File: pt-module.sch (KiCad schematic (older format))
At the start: 6 parts

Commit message: Added USB to UART interface
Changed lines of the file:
@@
 LIBS:switches
 LIBS:ESD_Protection
+LIBS:ftdi
 LIBS:pt-module-cache
 EELAYER 25 0
@@
 $Descr A4 11693 8268
 encoding utf-8
-Sheet 1 7
+Sheet 1 8
 Title "ProbeTester Module"
 Date ""
@@
 F4 "termination_logic" I R 9000 4200 60
 $EndSheet
+$Sheet
+S 5400 4550 600  550
+U 59836BB9
+F0 "PT module USB interface" 60
+F1 "pt-module-usb-interface.sch" 60
+$EndSheet
 $EndSCHEMATC

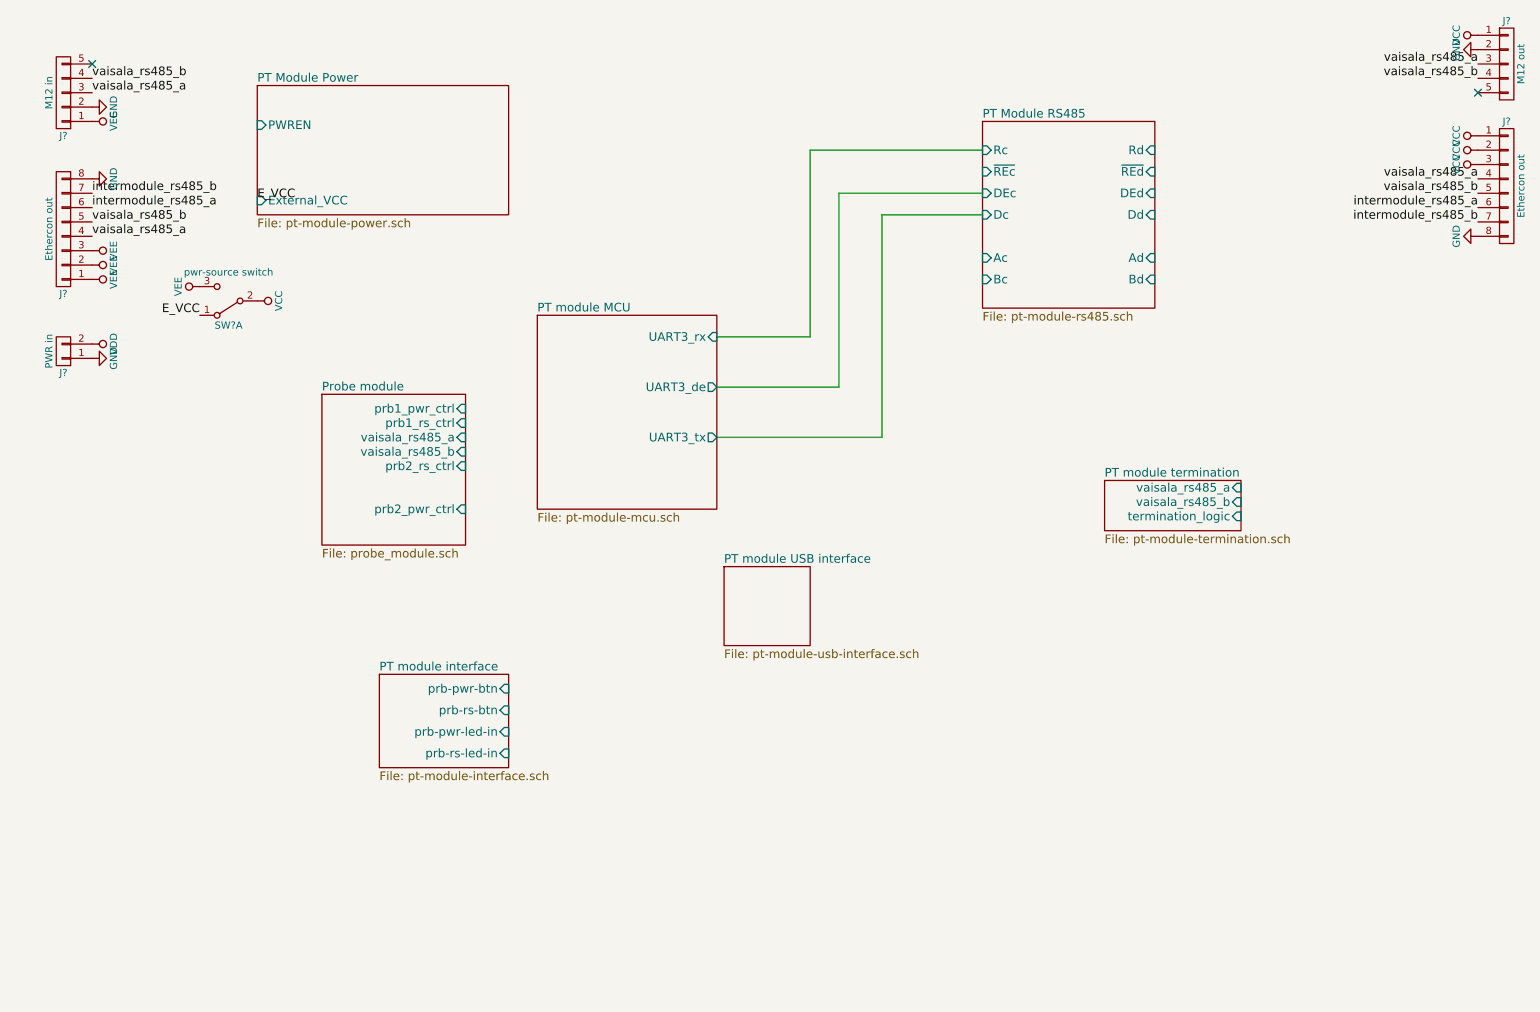
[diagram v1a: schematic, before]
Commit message: Added USB UART hierarchical connection
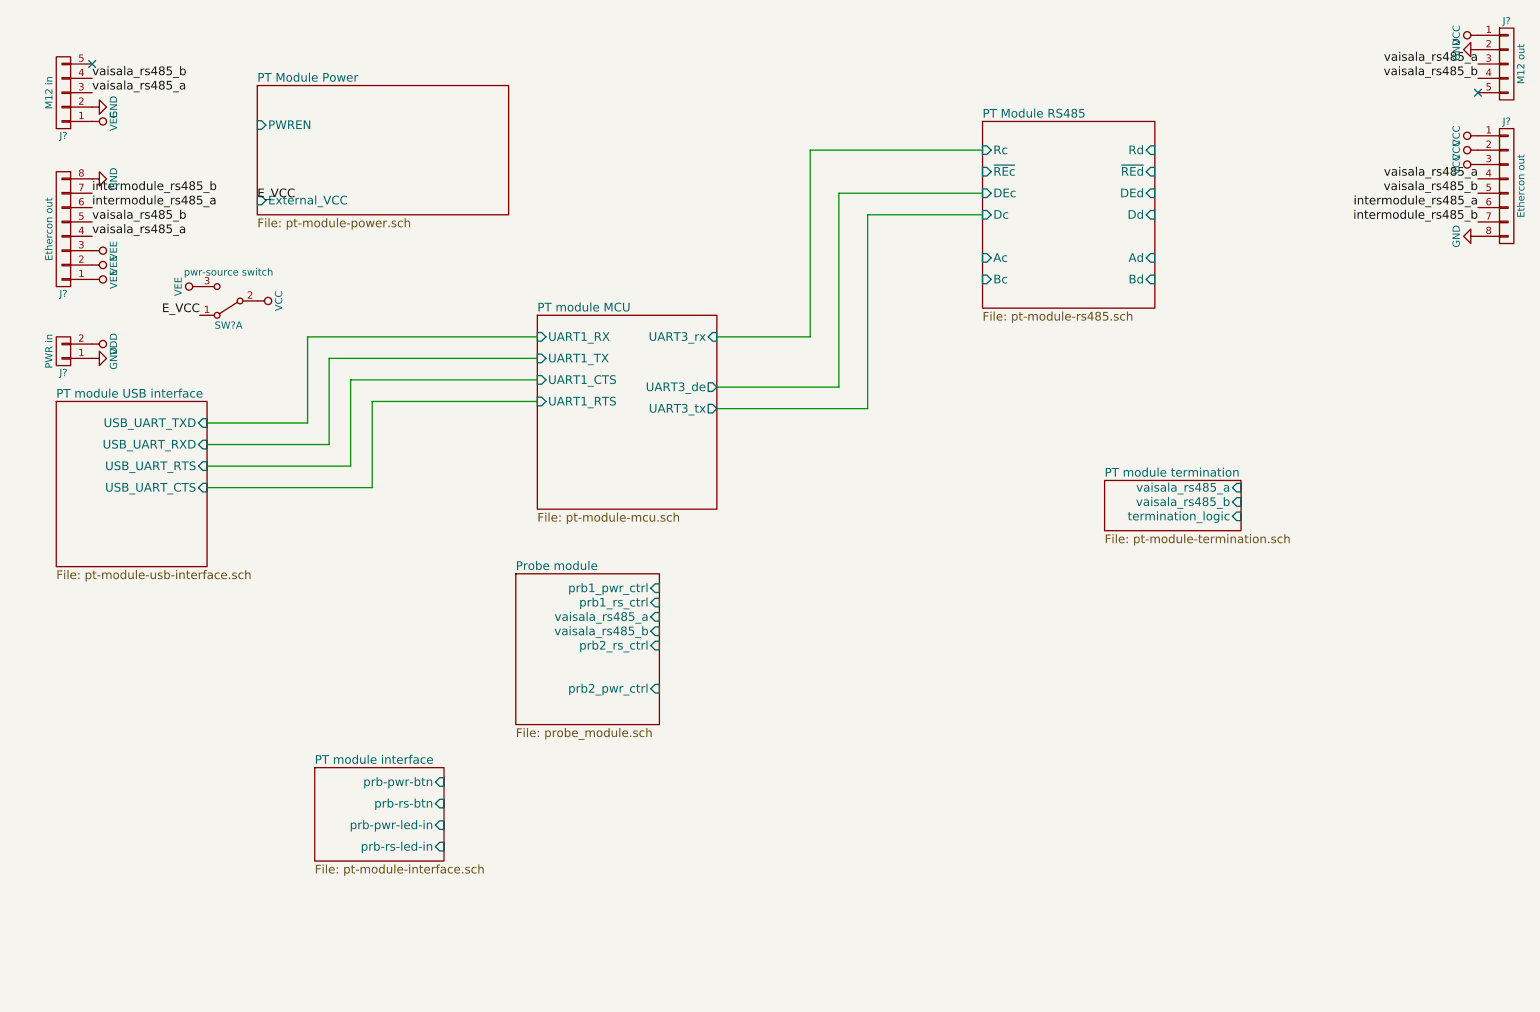
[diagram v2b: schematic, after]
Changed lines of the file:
@@
 F0 "PT module MCU" 60
 F1 "pt-module-mcu.sch" 60
-F2 "UART3_tx" O R 5350 3650 60
+F2 "UART3_tx" O R 5350 3450 60
 F3 "UART3_rx" I R 5350 2950 60
 F4 "UART3_de" O R 5350 3300 60
+F5 "UART1_TX" I L 4100 3100 60
+F6 "UART1_RX" I L 4100 2950 60
+F7 "UART1_CTS" I L 4100 3250 60
+F8 "UART1_RTS" I L 4100 3400 60
 $EndSheet
 $Sheet
-S 2600 3350 1000 1050
+S 3950 4600 1000 1050
 U 598183C5
 F0 "Probe module" 60
 F1 "probe_module.sch" 60
-F2 "prb1_pwr_ctrl" I R 3600 3450 60
-F3 "prb1_rs_ctrl" I R 3600 3550 60
-F4 "prb2_rs_ctrl" I R 3600 3850 60
-F5 "prb2_pwr_ctrl" I R 3600 4150 60
-F6 "vaisala_rs485_a" I R 3600 3650 60
-F7 "vaisala_rs485_b" I R 3600 3750 60
+F2 "prb1_pwr_ctrl" I R 4950 4700 60
+F3 "prb1_rs_ctrl" I R 4950 4800 60
+F4 "prb2_rs_ctrl" I R 4950 5100 60
+F5 "prb2_pwr_ctrl" I R 4950 5400 60
+F6 "vaisala_rs485_a" I R 4950 4900 60
+F7 "vaisala_rs485_b" I R 4950 5000 60
 $EndSheet
 $Sheet
-S 3000 5300 900  650
+S 2550 5950 900  650
 U 59819805
 F0 "PT module interface" 60
 F1 "pt-module-interface.sch" 60
-F2 "prb-pwr-btn" I R 3900 5400 60
-F3 "prb-rs-btn" I R 3900 5550 60
-F4 "prb-pwr-led-in" I R 3900 5700 60
-F5 "prb-rs-led-in" I R 3900 5850 60
+F2 "prb-pwr-btn" I R 3450 6050 60
+F3 "prb-rs-btn" I R 3450 6200 60
+F4 "prb-pwr-led-in" I R 3450 6350 60
+F5 "prb-rs-led-in" I R 3450 6500 60
 $EndSheet
 $Comp
@@
 	6000 1650 7200 1650
 Wire Wire Line
-	5350 3650 6500 3650
-Wire Wire Line
-	6500 3650 6500 2100
-Wire Wire Line
-	6500 2100 7200 2100
+	6400 2100 7200 2100
 Text Label 2150 2000 0    60   ~ 0
 E_VCC
@@
 $EndSheet
 $Sheet
-S 5400 4550 600  550
+S 750  3400 1050 1150
 U 59836BB9
 F0 "PT module USB interface" 60
 F1 "pt-module-usb-interface.sch" 60
-$EndSheet
+F2 "USB_UART_TXD" I R 1800 3550 60
+F3 "USB_UART_RXD" I R 1800 3700 60
+F4 "USB_UART_RTS" I R 1800 3850 60
+F5 "USB_UART_CTS" I R 1800 4000 60
+$EndSheet
+Wire Wire Line
+	6400 2100 6400 3450
+Wire Wire Line
+	6400 3450 5350 3450
+Wire Wire Line
+	2500 2950 4100 2950
+Wire Wire Line
+	2500 2950 2500 3550
+Wire Wire Line
+	2500 3550 1800 3550
+Wire Wire Line
+	4100 3100 2650 3100
+Wire Wire Line
+	2650 3100 2650 3700
+Wire Wire Line
+	2650 3700 1800 3700
+Wire Wire Line
+	4100 3250 2800 3250
+Wire Wire Line
+	2800 3250 2800 3850
+Wire Wire Line
+	2800 3850 1800 3850
+Wire Wire Line
+	4100 3400 2950 3400
+Wire Wire Line
+	2950 3400 2950 4000
+Wire Wire Line
+	2950 4000 1800 4000
 $EndSCHEMATC

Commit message: Added another rs485 link to MCU
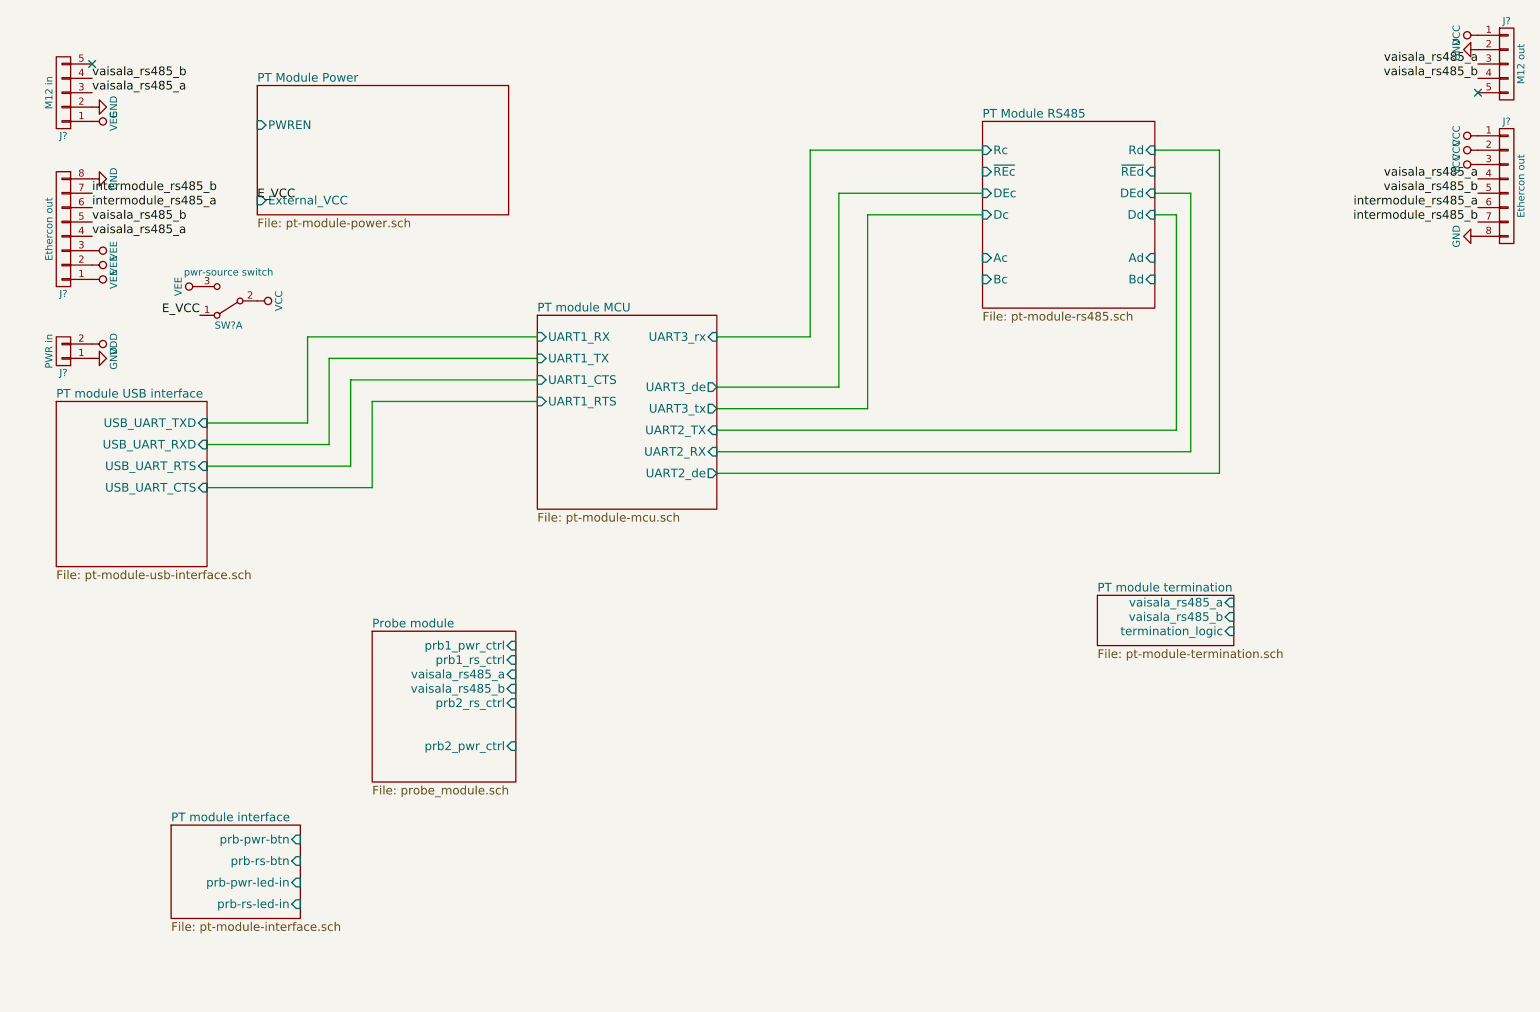
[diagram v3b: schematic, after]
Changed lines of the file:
@@
 F7 "UART1_CTS" I L 4100 3250 60
 F8 "UART1_RTS" I L 4100 3400 60
+F9 "UART2_RX" I R 5350 3750 60
+F10 "UART2_TX" I R 5350 3600 60
+F11 "UART2_de" O R 5350 3900 60
 $EndSheet
 $Sheet
-S 3950 4600 1000 1050
+S 2950 5000 1000 1050
 U 598183C5
 F0 "Probe module" 60
 F1 "probe_module.sch" 60
-F2 "prb1_pwr_ctrl" I R 4950 4700 60
-F3 "prb1_rs_ctrl" I R 4950 4800 60
-F4 "prb2_rs_ctrl" I R 4950 5100 60
-F5 "prb2_pwr_ctrl" I R 4950 5400 60
-F6 "vaisala_rs485_a" I R 4950 4900 60
-F7 "vaisala_rs485_b" I R 4950 5000 60
+F2 "prb1_pwr_ctrl" I R 3950 5100 60
+F3 "prb1_rs_ctrl" I R 3950 5200 60
+F4 "prb2_rs_ctrl" I R 3950 5500 60
+F5 "prb2_pwr_ctrl" I R 3950 5800 60
+F6 "vaisala_rs485_a" I R 3950 5300 60
+F7 "vaisala_rs485_b" I R 3950 5400 60
 $EndSheet
 $Sheet
-S 2550 5950 900  650
+S 1550 6350 900  650
 U 59819805
 F0 "PT module interface" 60
 F1 "pt-module-interface.sch" 60
-F2 "prb-pwr-btn" I R 3450 6050 60
-F3 "prb-rs-btn" I R 3450 6200 60
-F4 "prb-pwr-led-in" I R 3450 6350 60
-F5 "prb-rs-led-in" I R 3450 6500 60
+F2 "prb-pwr-btn" I R 2450 6450 60
+F3 "prb-rs-btn" I R 2450 6600 60
+F4 "prb-pwr-led-in" I R 2450 6750 60
+F5 "prb-rs-led-in" I R 2450 6900 60
 $EndSheet
 $Comp
@@
 $EndComp
 $Sheet
-S 8050 3950 950  350
+S 8000 4750 950  350
 U 5987986D
 F0 "PT module termination" 60
 F1 "pt-module-termination.sch" 60
-F2 "vaisala_rs485_a" I R 9000 4000 60
-F3 "vaisala_rs485_b" I R 9000 4100 60
-F4 "termination_logic" I R 9000 4200 60
+F2 "vaisala_rs485_a" I R 8950 4800 60
+F3 "vaisala_rs485_b" I R 8950 4900 60
+F4 "termination_logic" I R 8950 5000 60
 $EndSheet
 $Sheet
@@
 Wire Wire Line
 	2950 4000 1800 4000
+Wire Wire Line
+	8400 2100 8550 2100
+Wire Wire Line
+	8550 2100 8550 3600
+Wire Wire Line
+	8550 3600 5350 3600
+Wire Wire Line
+	5350 3750 8650 3750
+Wire Wire Line
+	8650 3750 8650 1950
+Wire Wire Line
+	8650 1950 8400 1950
+Wire Wire Line
+	5350 3900 8850 3900
+Wire Wire Line
+	8850 3900 8850 1650
+Wire Wire Line
+	8850 1650 8400 1650
 $EndSCHEMATC

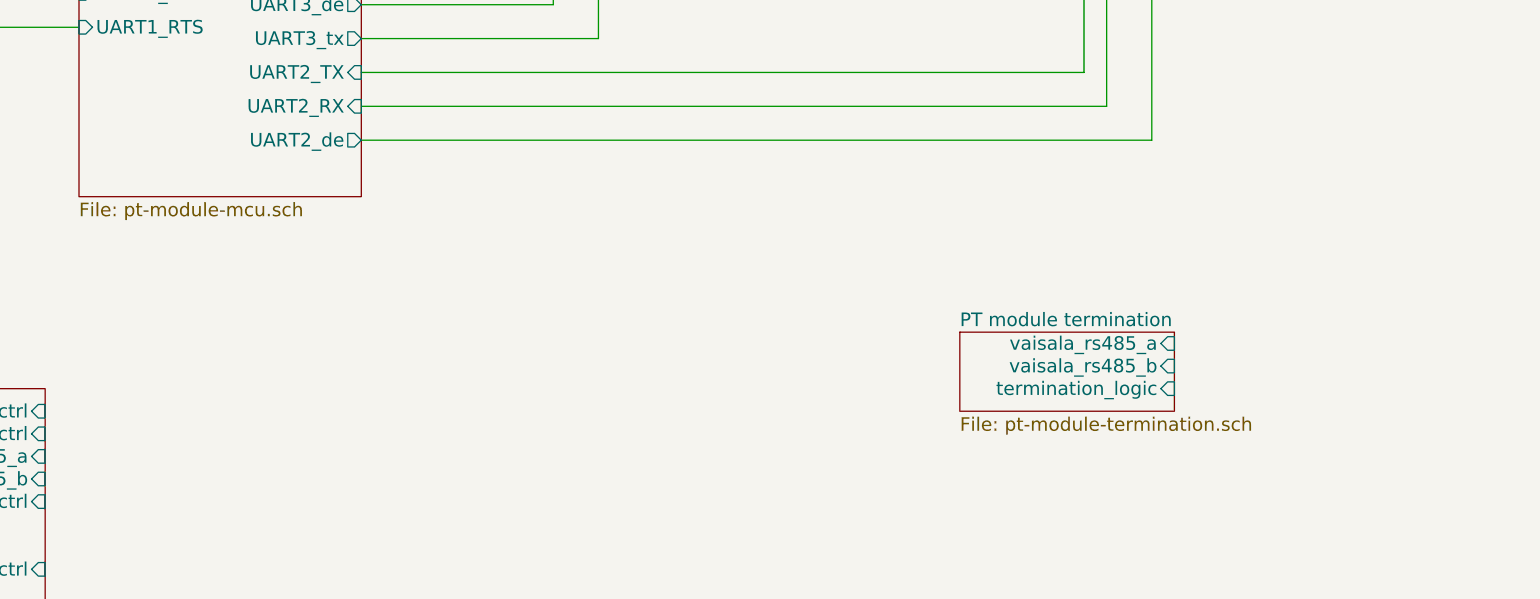
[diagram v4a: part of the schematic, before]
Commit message: Added resistor and capacitor values in MCU sheet.
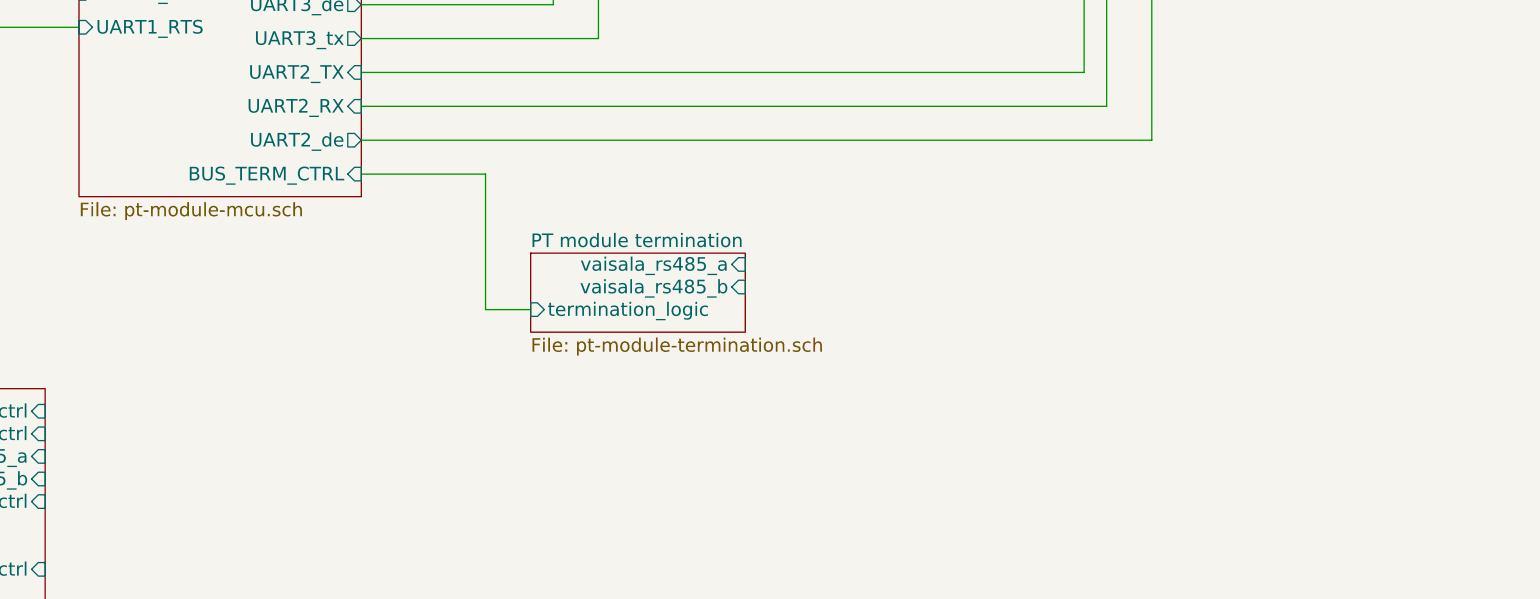
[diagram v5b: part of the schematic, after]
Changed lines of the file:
@@
 F10 "UART2_TX" I R 5350 3600 60
 F11 "UART2_de" O R 5350 3900 60
+F12 "BUS_TERM_CTRL" I R 5350 4050 60
 $EndSheet
 $Sheet
@@
 	-1   0    0    1
 $EndComp
+Wire Wire Line
+	5350 3300 6200 3300
+Wire Wire Line
+	6200 3300 6200 1950
+Wire Wire Line
+	6200 1950 7200 1950
+Wire Wire Line
+	5350 2950 6000 2950
+Wire Wire Line
+	6000 2950 6000 1650
+Wire Wire Line
+	6000 1650 7200 1650
+Wire Wire Line
+	6400 2100 7200 2100
 Text Label 2150 2000 0    60   ~ 0
 E_VCC
@@
 $EndComp
 $Sheet
-S 8000 4750 950  350
+S 6100 4400 950  350
 U 5987986D
 F0 "PT module termination" 60
 F1 "pt-module-termination.sch" 60
-F2 "vaisala_rs485_a" I R 8950 4800 60
-F3 "vaisala_rs485_b" I R 8950 4900 60
-F4 "termination_logic" I R 8950 5000 60
+F2 "vaisala_rs485_a" I R 7050 4450 60
+F3 "vaisala_rs485_b" I R 7050 4550 60
+F4 "termination_logic" I L 6100 4650 60
 $EndSheet
 $Sheet
@@
 $EndSheet
 Wire Wire Line
-	5350 3300 6200 3300
-Wire Wire Line
-	6200 3300 6200 1950
-Wire Wire Line
-	6200 1950 7200 1950
-Wire Wire Line
-	5350 2950 6000 2950
-Wire Wire Line
-	6000 2950 6000 1650
-Wire Wire Line
-	6000 1650 7200 1650
-Wire Wire Line
-	6400 2100 7200 2100
-Wire Wire Line
 	6400 2100 6400 3450
 Wire Wire Line
@@
 Wire Wire Line
 	8850 1650 8400 1650
+Wire Wire Line
+	5350 4050 5900 4050
+Wire Wire Line
+	5900 4050 5900 4650
+Wire Wire Line
+	5900 4650 6100 4650
 $EndSCHEMATC

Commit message: I made a connect
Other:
- moved on the sheet: J?, SW?A
